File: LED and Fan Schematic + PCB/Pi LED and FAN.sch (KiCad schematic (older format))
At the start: 15 parts, among them J1 GPIO Pin 4, J2 GPIO Pin 3, J3 5V_IN, J4 GND, M1 Fan, Q1 P2N2222A, Q2 P2N2222A

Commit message: began looking for components fo build BMS system
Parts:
- Q1, Q2: symbol P2N2222A:P2N2222A -> Pi-LED-and-FAN-rescue:P2N2222A-P2N2222A
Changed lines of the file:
@@
 $EndComp
 $Comp
-L P2N2222A:P2N2222A Q2
+L Pi-LED-and-FAN-rescue:P2N2222A-P2N2222A Q2
 U 1 1 5D47A305
 P 7900 4850
@@
 	5100 2750 8000 2750
 $Comp
-L P2N2222A:P2N2222A Q1
+L Pi-LED-and-FAN-rescue:P2N2222A-P2N2222A Q1
 U 1 1 5D488AA0
 P 5000 4850

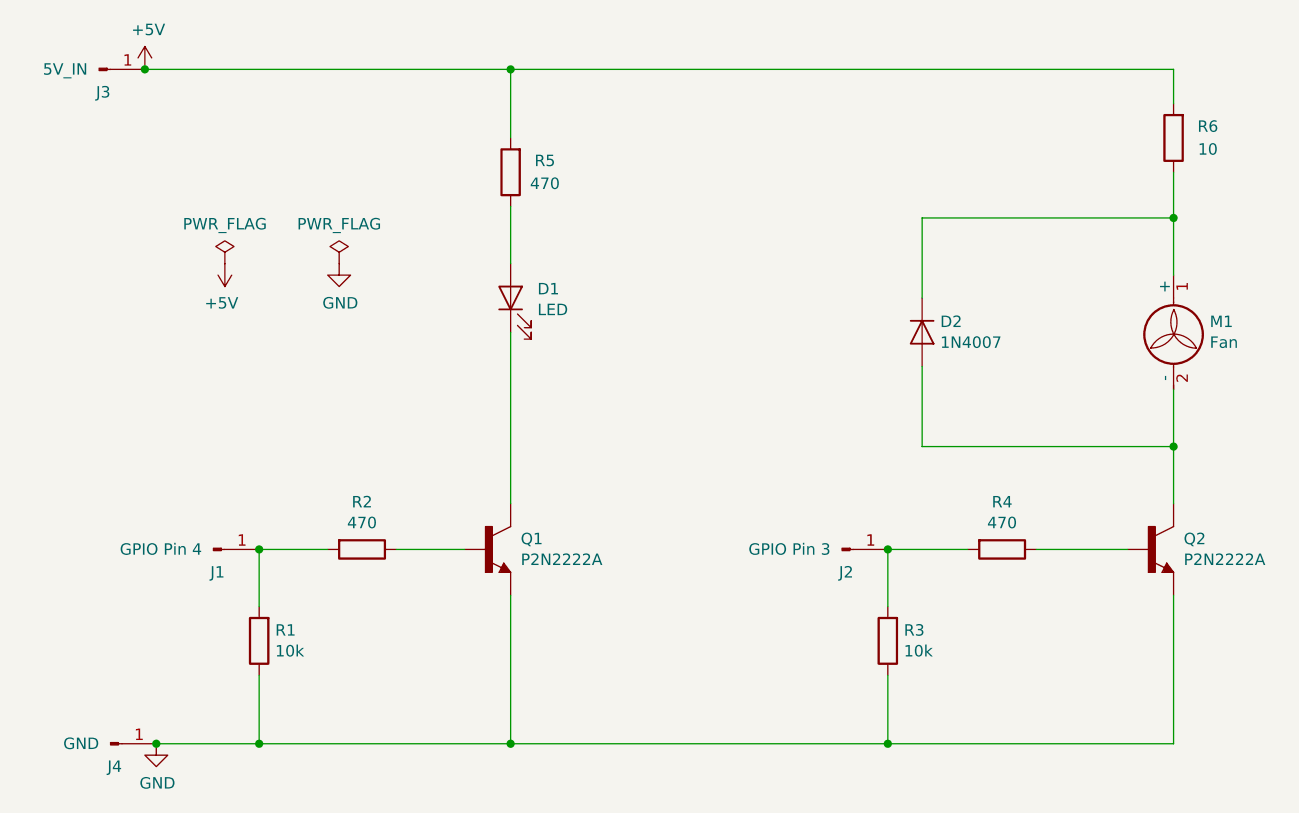
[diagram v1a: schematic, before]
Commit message: made some changes to PCB schematic and code updated for new GPIO Pins
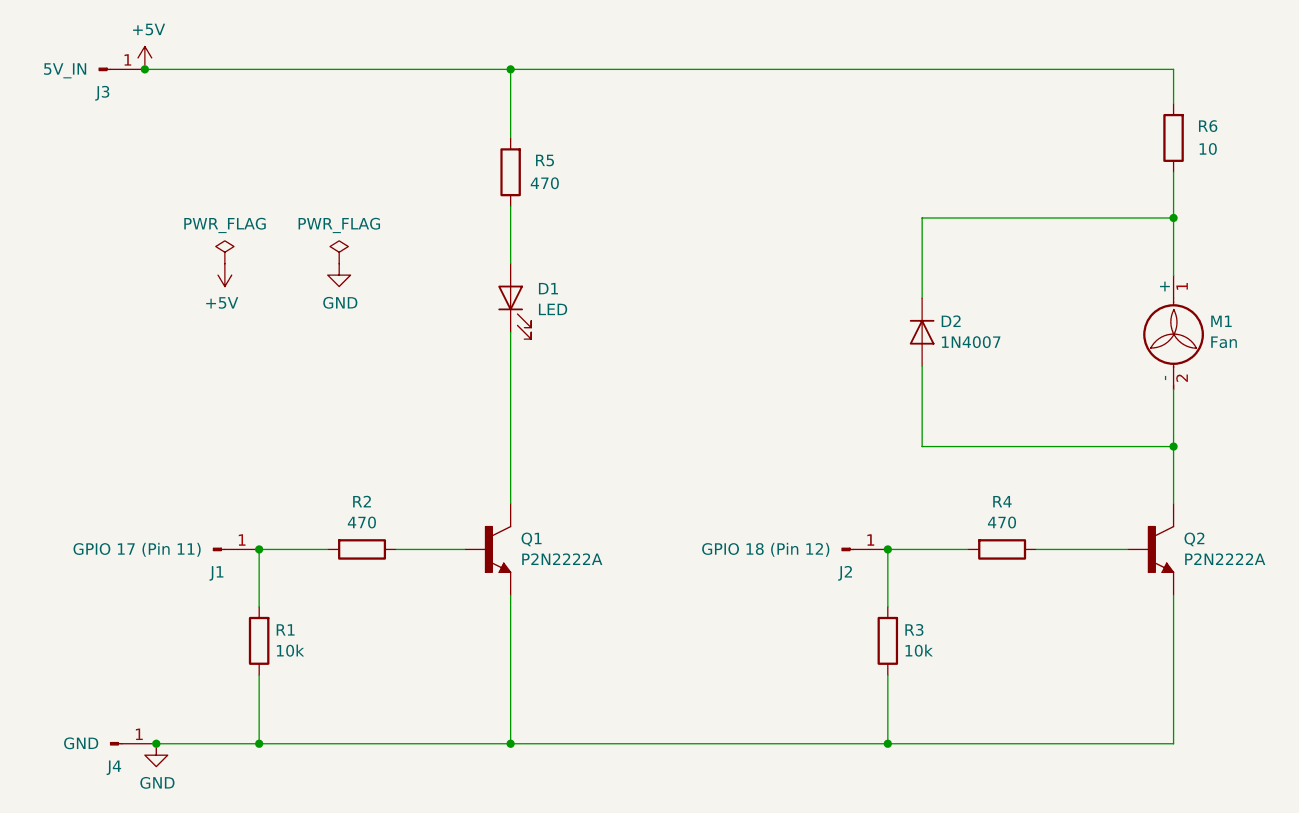
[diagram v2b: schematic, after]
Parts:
- J1: value GPIO Pin 4 -> GPIO 17 (Pin 11)
- J2: value GPIO Pin 3 -> GPIO 18 (Pin 12)
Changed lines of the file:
@@
 P 6550 4850
 F 0 "J2" H 6600 4750 50  0000 R CNN
-F 1 "GPIO Pin 3" H 6500 4850 50  0000 R CNN
+F 1 "GPIO 18 (Pin 12)" H 6500 4850 50  0000 R CNN
 F 2 "Connector_PinHeader_2.54mm:PinHeader_1x01_P2.54mm_Vertical" H 6550 4850 50  0001 C CNN
 F 3 "~" H 6550 4850 50  0001 C CNN
@@
 P 3800 4850
 F 0 "J1" H 3850 4750 50  0000 R CNN
-F 1 "GPIO Pin 4" H 3750 4850 50  0000 R CNN
+F 1 "GPIO 17 (Pin 11)" H 3750 4850 50  0000 R CNN
 F 2 "Connector_PinHeader_2.54mm:PinHeader_1x01_P2.54mm_Vertical" H 3800 4850 50  0001 C CNN
 F 3 "~" H 3800 4850 50  0001 C CNN
